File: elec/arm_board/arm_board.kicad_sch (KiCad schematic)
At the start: 34 parts, among them J1 PinHeader, J12 B2B-XH-A(LF)(SN), J16 B4B-ZR(LF)(SN), J2 PinHeader, J3 B6B-ZR, J4 Fan motor, Q1 NMOS, SW1 B3U-3000P, U1 NA219AIDR, U12 OKL-T/6-W12N-C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

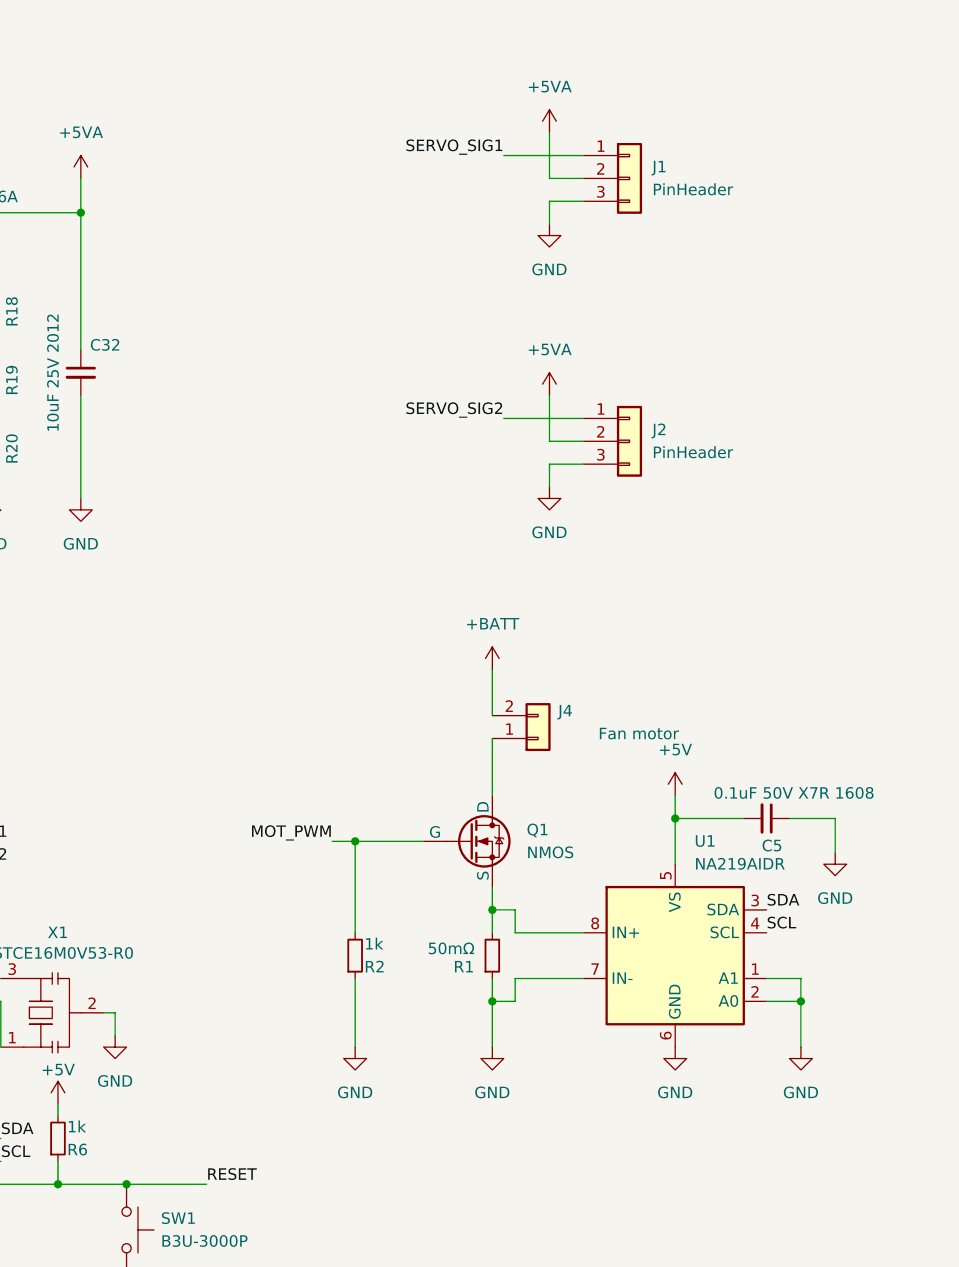
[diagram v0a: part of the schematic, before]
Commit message: アームボードのモータードライバを変更
Signed-off-by: Kazuki Iida <elkel53930@gmail.com>
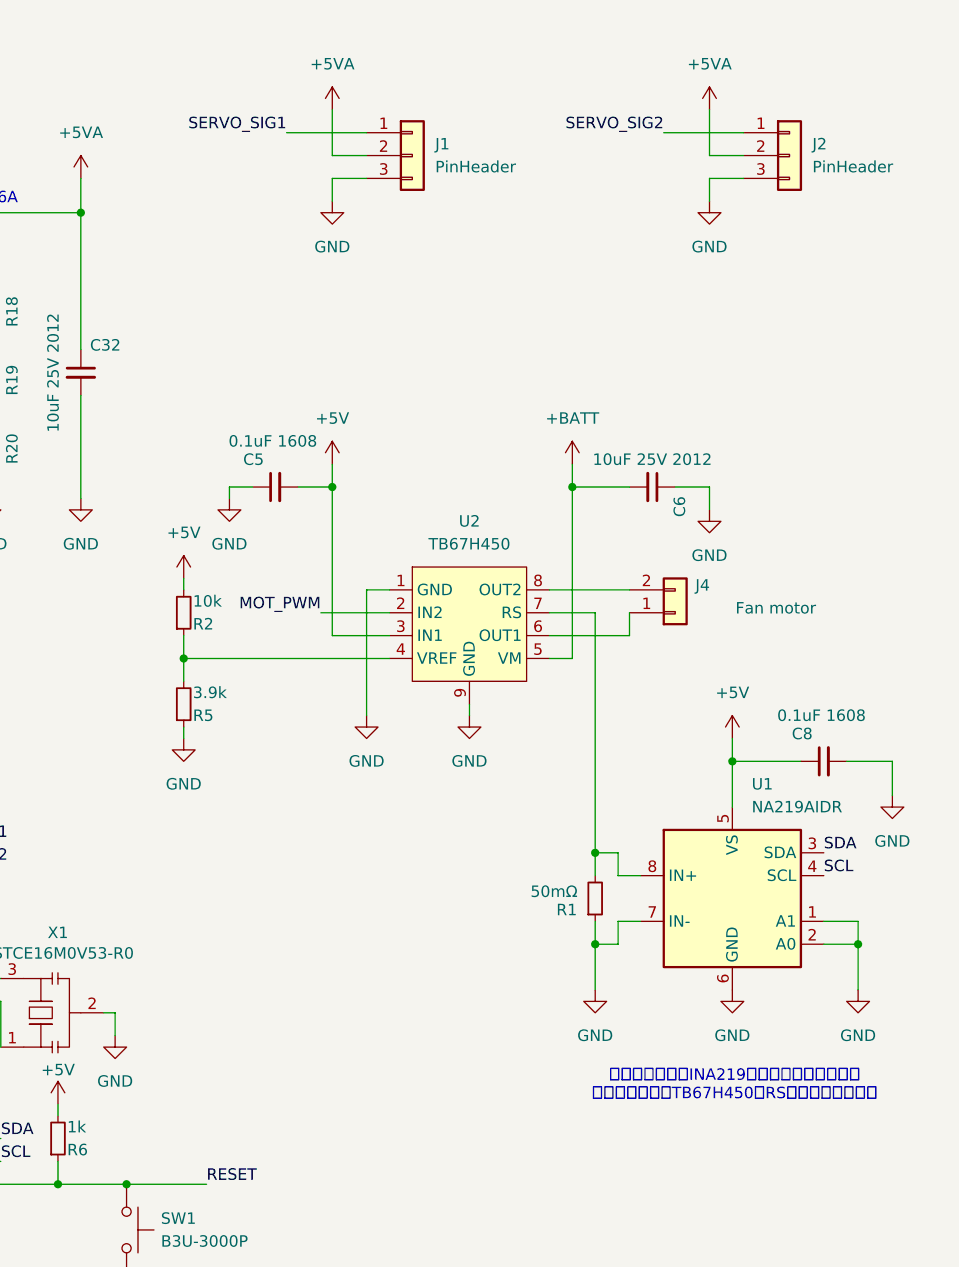
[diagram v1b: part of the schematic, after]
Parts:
- removed Q1: NMOS, symbol Simulation_SPICE:NMOS
- added C6: CL21A106KAYNNNE, Capacitor_SMD:C_0805_2012Metric, symbol Device:C_Small
- added C8: CC0603KRX7R9BB104, Capacitor_SMD:C_0603_1608Metric, symbol Device:C_Small
- added R5: 3.9k, Resistor_SMD:R_0603_1608Metric, symbol Device:R_Small
- added U2: TB67H450, Package_SO:HSOP-8-1EP_3.9x4.9mm_P1.27mm_EP2.3x2.3mm, symbol micromouse-twilight:TB67H450
- R2: value 1k -> 10k
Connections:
- net +5V: now also R2.2, C8.1, U2.3 (IN1)
- net +BATT: now also C6.2, U2.5 (VM); no longer J4.2 (Pin_2)
- net GND: now also C6.1, C8.2, R5.1, U2.1 (GND), U2.9 (GND); no longer R2.1
- net MOT_PWM: now also U2.2 (IN2); no longer R2.2
- net at R1.2, U1.8 (IN+): now also U2.7 (RS)
- net at J4.1 (Pin_1): now also U2.6 (OUT1)
- new net: R2.1, R5.2, U2.4 (VREF)
- new net: J4.2 (Pin_2), U2.8 (OUT2)
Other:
- note added: "電流検出抵抗とINA219の間はケルビン接続。 電流検出抵抗はTB67H450のRSピン直近に配置。"
- moved on the sheet: J1, J2, J4, R1, U1

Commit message: 抵抗などの型番を指定
Signed-off-by: Kazuki Iida <elkel53930@gmail.com>
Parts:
- removed R9: 1k, Resistor_SMD:R_0603_1608Metric, symbol Device:R_Small
- added R7: 0603WAF1001T5E, Resistor_SMD:R_0603_1608Metric, symbol Device:R_Small
- R2: value 10k -> 0603WAF1002T5E
- R3, R4, R6, R8: value 1k -> 0603WAF1001T5E
- R5: value 3.9k -> 0603WAF3901T5E
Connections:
- net RX: now also R7.1; no longer R8.2
- net TX: now also R8.1
- net at U3.30 (PD0): now also R7.2; no longer R8.1
- net at U3.31 (PD1): now also R8.2

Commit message: ARMボード発注
Signed-off-by: Kazuki Iida <elkel53930@gmail.com>
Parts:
- removed C5: CC0603KRX7R9BB104, Capacitor_SMD:C_0603_1608Metric, symbol Device:C_Small
- removed R18: 0603WAF1001T5E, Resistor_SMD:R_0603_1608Metric, symbol Device:R
- removed R19: 0603WAF3300T5E, Resistor_SMD:R_0603_1608Metric, symbol Device:R
- removed R20: 0603WAF100JT5E, Resistor_SMD:R_0603_1608Metric, symbol Device:R
- removed U12: OKL-T/6-W12N-C, Library:OKL-T&slash_6-W12N-C_MUR, symbol micromouse-twilight:OKL-T/6-W12N-C
- added C10: CC0603KRX7R9BB104, Capacitor_SMD:C_0603_1608Metric, symbol Device:C_Small
- added C5, C9: RVT1A101M0505, Capacitor_SMD:CP_Elec_5x5.4, symbol Device:C_Polarized_Small
- added D1: WS2812B-2020, LED_SMD:LED_WS2812B-2020_PLCC4_2.0x2.0mm, symbol LED:WS2812B-2020
- added D2: D-060306G1/SS2/G1, LED_SMD:LED_0603_1608Metric, symbol Device:LED
- added H1, H2: M2, MountingHole:MountingHole_2.2mm_M2, symbol Mechanical:MountingHole
- added H3: M3, MountingHole:MountingHole_3.2mm_M3, symbol Mechanical:MountingHole
- added J5: Fan motor, Connector_PinHeader_2.54mm:PinHeader_1x02_P2.54mm_Vertical, symbol Connector_Generic:Conn_01x02
- added J6: B2B-XH-A(LF)(SN), Connector_JST:JST_XH_B2B-XH-AM_1x02_P2.50mm_Vertical, symbol Connector_Generic:Conn_01x02
- added Q5: DMT6008LFG, Package_SON:Diodes_PowerDI3333-8, symbol Transistor_FET:DMT6008LFG
- added R10, R11: 0603WAF1002T5E, Resistor_SMD:R_0603_1608Metric, symbol Device:R
- added R12, R9: 0603WAF1001T5E, Resistor_SMD:R_0603_1608Metric, symbol Device:R_Small
- added U4: AMS1117-5.0, Package_TO_SOT_SMD:SOT-223-3_TabPin2, symbol Regulator_Linear:AMS1117-5.0
- X1: footprint Ceralock:CSTCE -> Crystal:Resonator_SMD_Murata_CSTxExxV-3Pin_3.0x1.1mm
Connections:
- net +5V: now also J3.6 (Pin_6), C10.1, D1.4 (VDD), J6.1 (Pin_1)
- net +5VA: now also C5.1, C9.1, U4.2 (VO)
- net +BATT: now also J5.2 (Pin_2), R10.2, R11.2, U4.3 (VI)
- net GND: now also C10.2, C5.2, C9.2, D1.2 (VSS), D2.1 (K), J6.2 (Pin_2), R12.1, R9.1, U4.1 (GND)
- net MOSI: now also J3.2 (Pin_2), Q5.4 (G), R9.2; no longer J3.4 (Pin_4)
- net RESET: now also J3.5 (Pin_5); no longer J3.6 (Pin_6)
- net SCK: now also J3.4 (Pin_4); no longer J3.5 (Pin_5)
- net VMON: now also R11.1, R12.2
- net LED_SIG: now reaches U3.10 (PD6)
- net LED_SIG: now also D1.3 (DIN)
- net RS: now reaches R1.2, U1.8 (IN+), U2.7 (RS)
- net RS: now also Q5.1 (S), Q5.2 (S), Q5.3 (S)
- net CS: no longer names the net of U3.14 (PB2)
- net CS: no longer J3.2 (Pin_2)
- net LED1: no longer names the net of U3.2 (PD4)
- new net: J5.1 (Pin_1), Q5.5 (D)
- new net: D2.2 (A), R10.1
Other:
- note added: "IN1 IN2 OUT1 OUT2 L L OFF OFF STOP H L H L CW L H L H CCW H H L L BRAKE"
- note added: "MOSI(D11)はTimer2 によるPWM信号と兼用。"
- note added: "Timer2はMOSIとMOT_PWMからの PWM信号生成に使用するため、 Arduinoのtone()は使用不可。"
- note added: "ブートローダー書込み用"
- note removed: "5V Max6A"
- note removed: "D10"
- moved on the sheet: C1, C2, C26, C3, C32, C38, C4, C41, C6, C7, C8, D4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

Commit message: ARMボードから不要な回路を削除
Signed-off-by: Kazuki Iida <elkel53930@gmail.com>
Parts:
- removed C6: CL21A106KAYNNNE, Capacitor_SMD:C_0805_2012Metric, symbol Device:C_Small
- removed J4: Fan motor, Connector_PinHeader_2.54mm:PinHeader_1x02_P2.54mm_Vertical, symbol Connector_Generic:Conn_01x02
- removed J6: B2B-XH-A(LF)(SN), Connector_JST:JST_XH_B2B-XH-AM_1x02_P2.50mm_Vertical, symbol Connector_Generic:Conn_01x02
- removed R10, R11: 0603WAF1002T5E, Resistor_SMD:R_0603_1608Metric, symbol Device:R
- removed SW1: B3U-3000P, Button_Switch_SMD:SW_SPST_B3U-3000P-B, symbol Switch:SW_Push
- removed U2: TB67H450, Package_SO:HSOP-8-1EP_3.9x4.9mm_P1.27mm_EP2.3x2.3mm, symbol micromouse-twilight:TB67H450
- added JP1: Switch 5V supply, Connector_PinHeader_1.00mm:PinHeader_1x02_P1.00mm_Vertical, symbol Jumper:Jumper_2_Bridged
- R5: value 0603WAF3901T5E -> 0603WAF1002T5E
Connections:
- net +5V: now also JP1.2 (B); no longer R2.2
- net +5VA: now also JP1.1 (A)
- net +BATT: now also R2.2, R5.2
- net GND: no longer R5.1
- net MOSI: no longer Q5.4 (G), R9.2
- net MOT_PWM: now also Q5.4 (G), R9.2
- net VMON: now also R5.1
- net at R2.1: now also D2.2 (A); no longer R5.2
- net RS: no longer names the net of Q5.1 (S), Q5.2 (S), Q5.3 (S), R1.2, U1.8 (IN+)
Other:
- note added: "Timer2はMOT_PWMからの PWM信号生成に使用するため、 Arduinoのtone()は使用不可。"
- note removed: "IN1 IN2 OUT1 OUT2 L L OFF OFF STOP H L H L CW L H L H CCW H H L L BRAKE"
- note removed: "MOSI(D11)はTimer2 によるPWM信号と兼用。"
- note removed: "Timer2はMOSIとMOT_PWMからの PWM信号生成に使用するため、 Arduinoのtone()は使用不可。"
- moved on the sheet: C5, C8, C9, D2, J1, J12, J2, J5, Q5, R1, R12, R9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

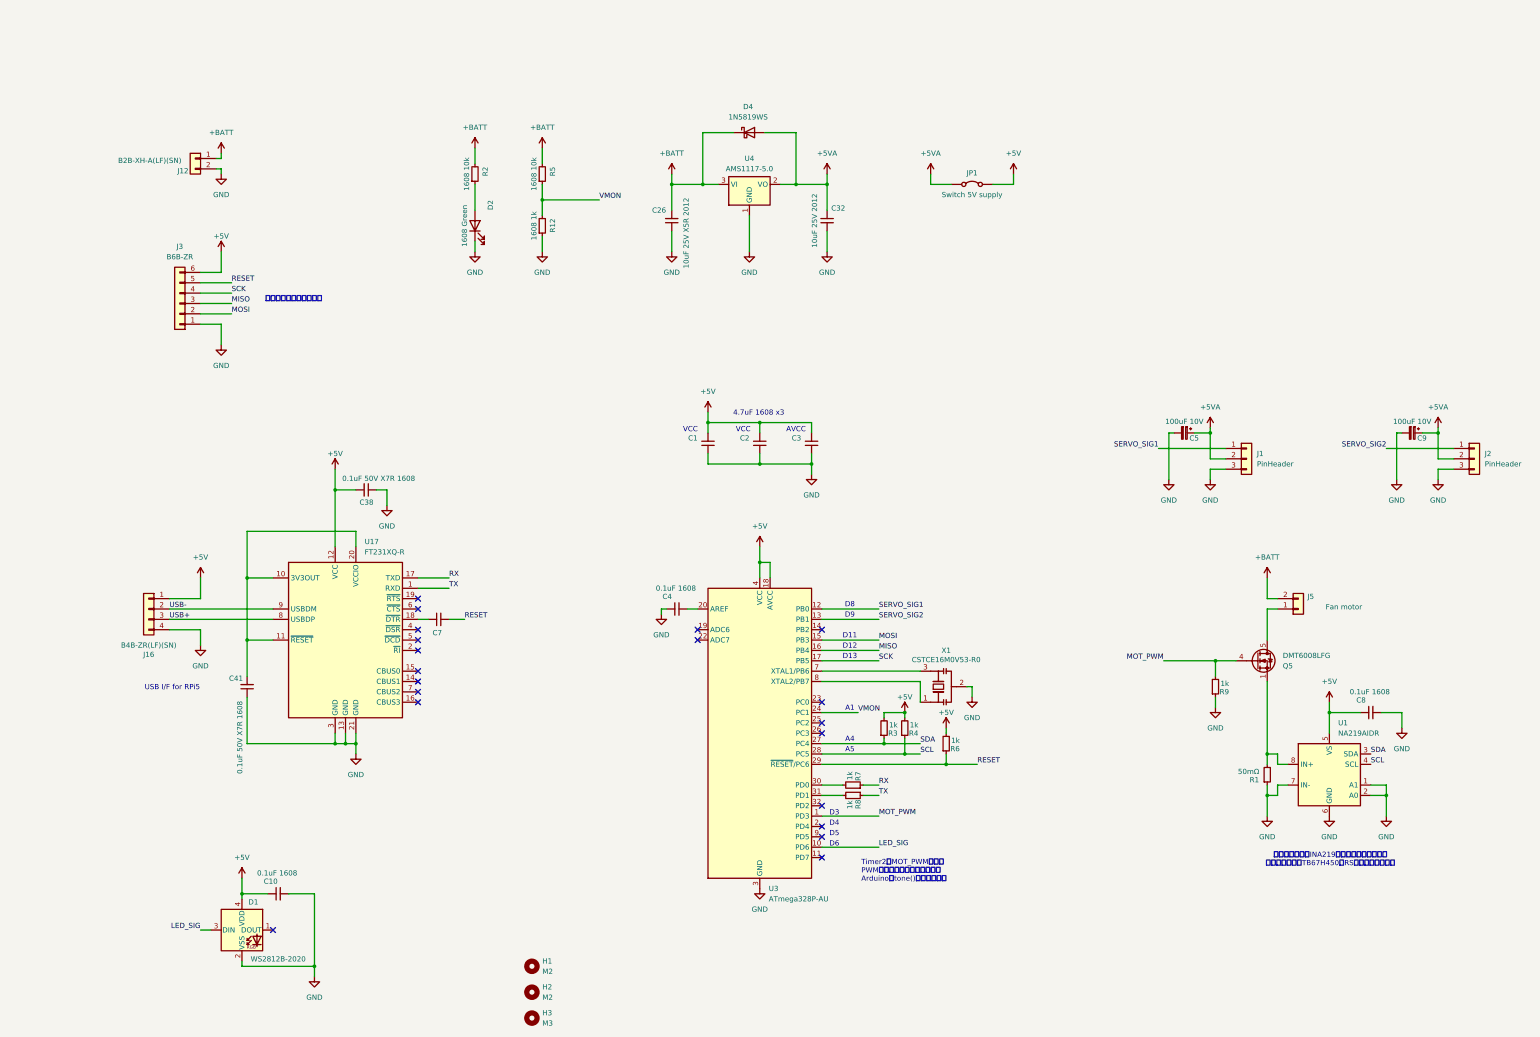
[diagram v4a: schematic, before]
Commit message: アーム基板v2の回路図＆アートワーク
Signed-off-by: Kazuki Iida <elkel53930@gmail.com>
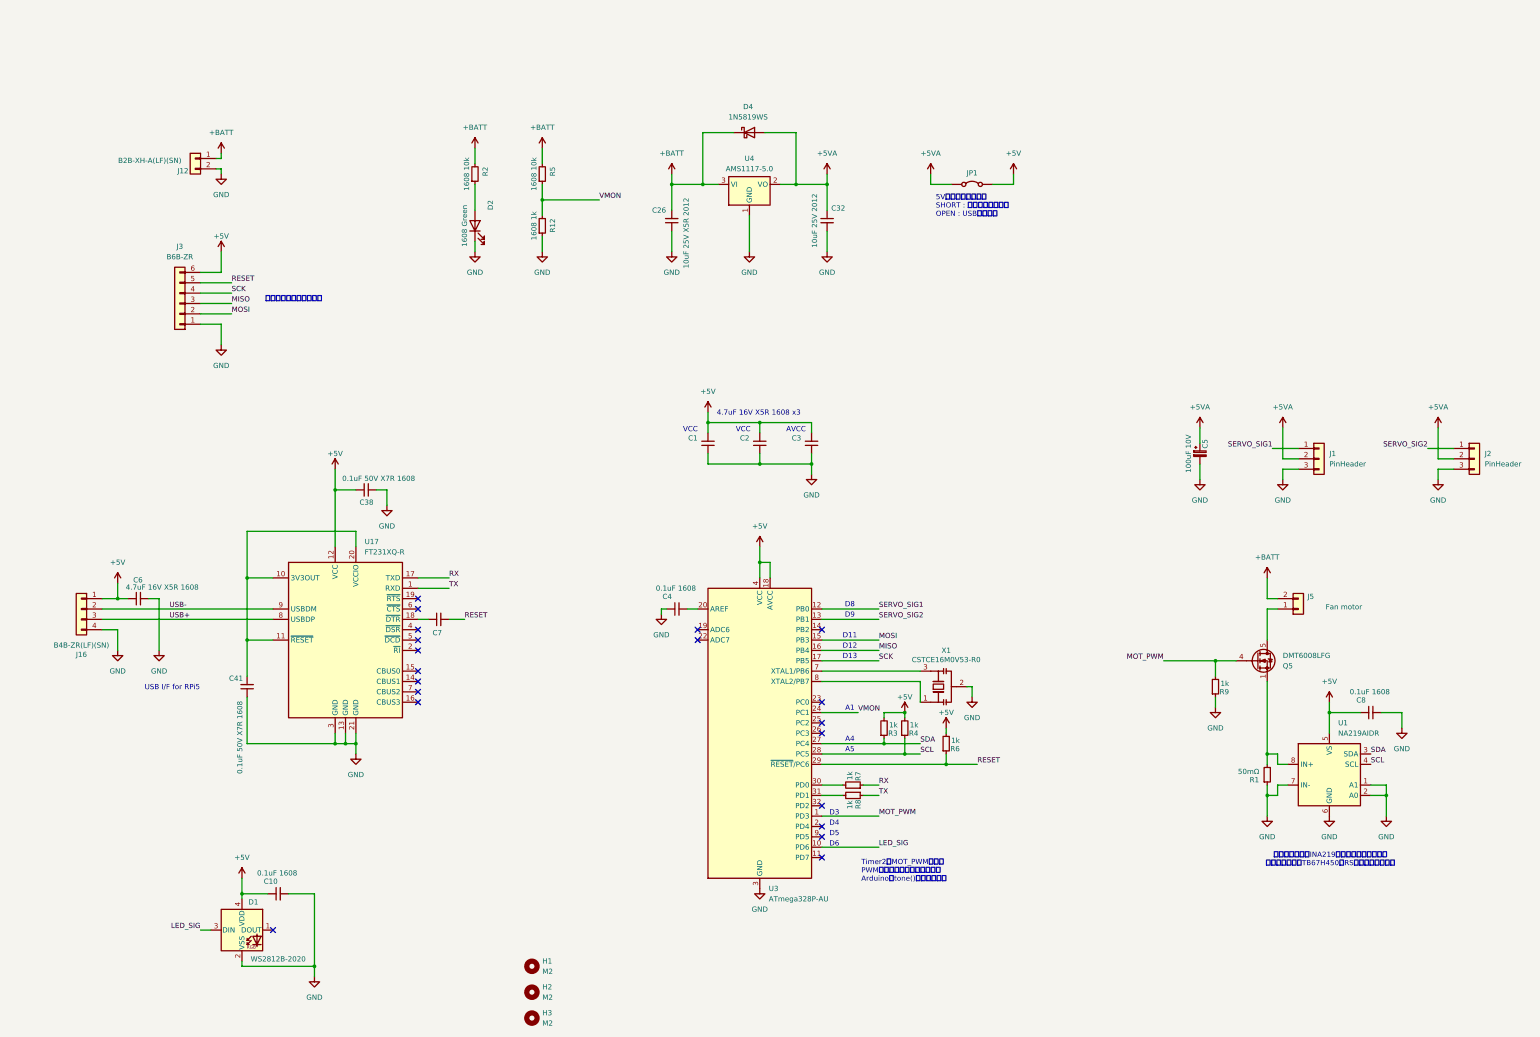
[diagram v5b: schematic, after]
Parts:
- removed C9: RVT1A101M0505, Capacitor_SMD:CP_Elec_5x5.4, symbol Device:C_Polarized_Small
- added C6: CL10A475KO8NNNC, Capacitor_SMD:C_0603_1608Metric, symbol Device:C_Small
- H3: value M3 -> M2; footprint MountingHole:MountingHole_3.2mm_M3 -> MountingHole:MountingHole_2.2mm_M2
- JP1: footprint Connector_PinHeader_1.00mm:PinHeader_1x02_P1.00mm_Vertical -> Connector_PinHeader_2.54mm:PinHeader_1x02_P2.54mm_Vertical
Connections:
- net +5V: now also C6.1
- net GND: now also C6.2
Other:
- note added: "4.7uF 16V X5R 1608 x3"
- note added: "5V電源の切り替え。 SHORT : 内蔵レギュレータ OPEN : USBコネクタ"
- note removed: "4.7uF 1608 x3"
- moved on the sheet: C5, J1, J16
